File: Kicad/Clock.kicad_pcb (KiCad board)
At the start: 2 copper layers, 99 x 57.5 mm, 42 parts, among them J1 AVR-ISP-6, J2 USB_B_Micro, Q5 BC848, Q6 BC848C, Q7 BC858A, SW1 Inc, SW2 Prgm, U1 KCSC02-123, U2 KCSC02-123, U3 KCSC02-123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

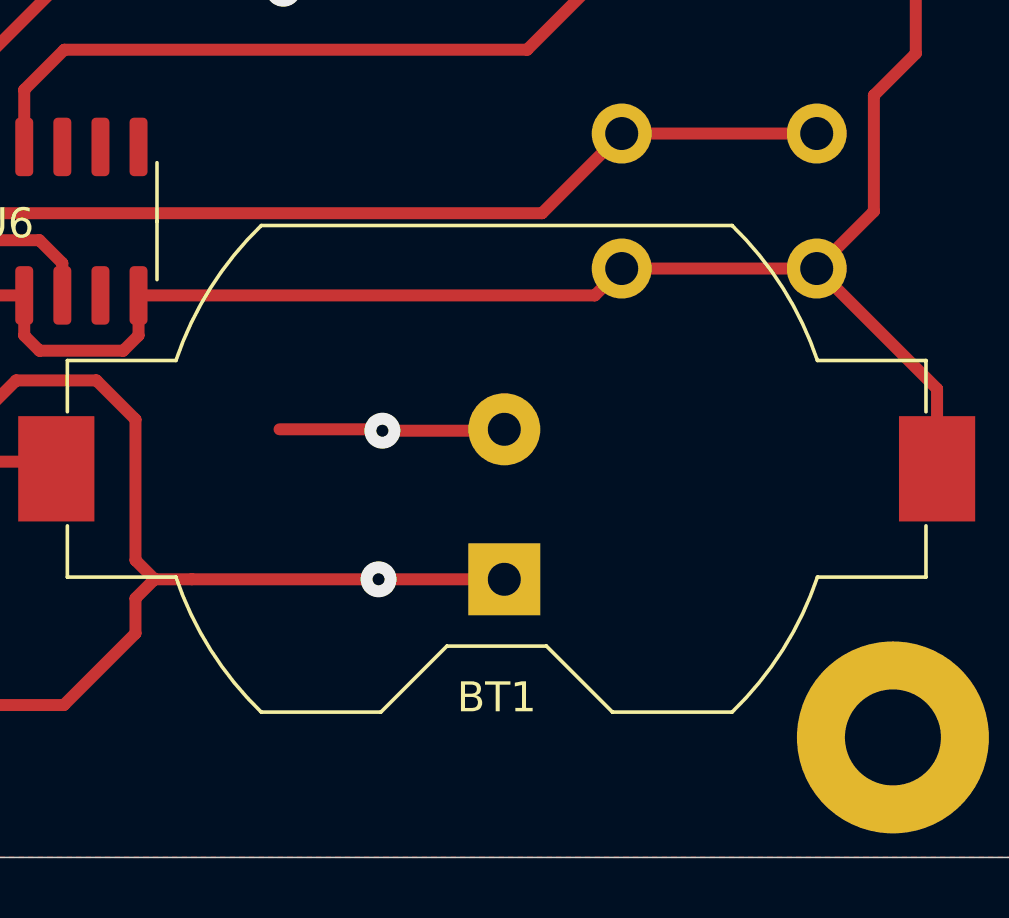
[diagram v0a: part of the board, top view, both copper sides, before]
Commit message: Flip Supercap to other board side
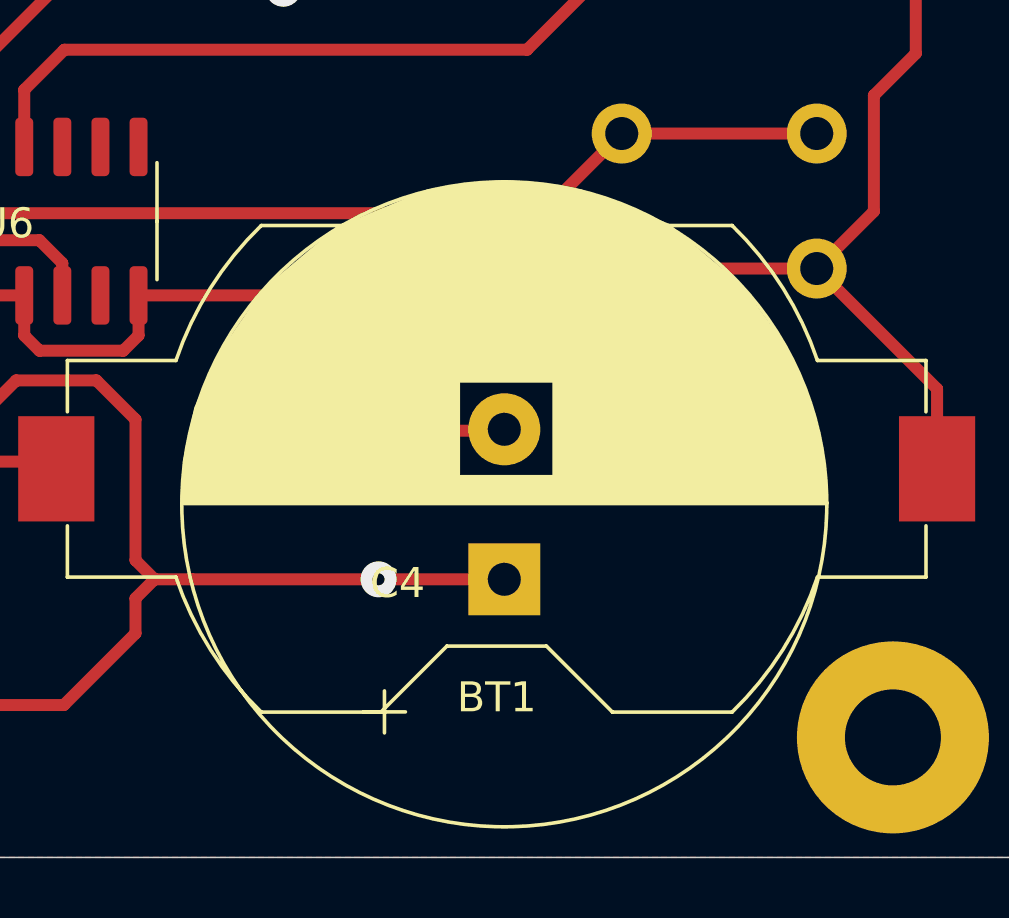
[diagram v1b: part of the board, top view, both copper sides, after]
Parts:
- C4: moved to F.Cu
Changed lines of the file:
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@@
     )
   )
-  (module Capacitor_THT:CP_Radial_D14.0mm_P5.00mm (layer B.Cu)
+  (module Capacitor_THT:CP_Radial_D14.0mm_P5.00mm (layer F.Cu)
     (at 148.3995 118.0465 90)
     (descr "CP, Radial series, Radial, pin pitch=5.00mm, , diameter=14mm, Electrolytic Capacitor")
     (tags "CP Radial series Radial pin pitch 5.00mm  diameter 14mm Electrolytic Capacitor")
-    (fp_text reference C4 (at -0.127 3.556) (layer B.SilkS)
-      (effects (font (size 1 1) (thickness 0.15)) (justify mirror))
+    (fp_text reference C4 (at -0.127 -3.556) (layer F.SilkS)
+      (effects (font (size 1 1) (thickness 0.15)))
     )
-    (fp_text value 1F (at 2.5 -8.25 270) (layer B.Fab)
-      (effects (font (size 1 1) (thickness 0.15)) (justify mirror))
+    (fp_text value 1F (at 2.5 8.25 90) (layer F.Fab)
+      (effects (font (size 1 1) (thickness 0.15)))
     )
-    (fp_line (start -4.419543 4.695) (end -4.419543 3.295) (layer B.SilkS) (width 0.12))
-    (fp_line (start -5.119543 3.995) (end -3.719543 3.995) (layer B.SilkS) (width 0.12))
-    (fp_line (start -2.813066 3.7675) (end -2.813066 2.3675) (layer B.Fab) (width 0.1))
-    (fp_line (start -3.513066 3.0675) (end -2.113066 3.0675) (layer B.Fab) (width 0.1))
-    (fp_circle (center 2.5 0) (end 13.5 0) (layer B.CrtYd) (width 0.05))
-    (fp_circle (center 2.5 0) (end 13.25 0) (layer B.SilkS) (width 0.12))
-    (fp_circle (center 2.5 0) (end 13 0) (layer B.Fab) (width 0.1))
-    (fp_line (start 2.54 10.668) (end 2.54 -10.75) (layer B.SilkS) (width 0.15))
-    (fp_poly (pts (xy 6.604 1.524) (xy 2.54 1.524) (xy 2.54 10.668) (xy 3.937 10.668)
-      (xy 5.715 10.287) (xy 7.62 9.398) (xy 9.652 8.001) (xy 11.684 5.588)
-      (xy 12.954 2.54) (xy 13.25 0) (xy 12.954 -2.54) (xy 11.811 -5.461)
-      (xy 9.779 -7.874) (xy 7.874 -9.271) (xy 5.969 -10.16) (xy 3.683 -10.668)
-      (xy 2.54 -10.668) (xy 2.54 -1.651) (xy 2.54 1.4732) (xy 3.429 1.4478)
-      (xy 3.429 -1.651) (xy 6.604 -1.651)) (layer B.SilkS) (width 0.1))
+    (fp_line (start -4.419543 -4.695) (end -4.419543 -3.295) (layer F.SilkS) (width 0.12))
+    (fp_line (start -5.119543 -3.995) (end -3.719543 -3.995) (layer F.SilkS) (width 0.12))
+    (fp_line (start -2.813066 -3.7675) (end -2.813066 -2.3675) (layer F.Fab) (width 0.1))
+    (fp_line (start -3.513066 -3.0675) (end -2.113066 -3.0675) (layer F.Fab) (width 0.1))
+    (fp_circle (center 2.5 0) (end 13.5 0) (layer F.CrtYd) (width 0.05))
+    (fp_circle (center 2.5 0) (end 13.25 0) (layer F.SilkS) (width 0.12))
+    (fp_circle (center 2.5 0) (end 13 0) (layer F.Fab) (width 0.1))
+    (fp_line (start 2.54 -10.668) (end 2.54 10.75) (layer F.SilkS) (width 0.15))
+    (fp_poly (pts (xy 6.604 -1.524) (xy 2.54 -1.524) (xy 2.54 -10.668) (xy 3.937 -10.668)
+      (xy 5.715 -10.287) (xy 7.62 -9.398) (xy 9.652 -8.001) (xy 11.684 -5.588)
+      (xy 12.954 -2.54) (xy 13.25 0) (xy 12.954 2.54) (xy 11.811 5.461)
+      (xy 9.779 7.874) (xy 7.874 9.271) (xy 5.969 10.16) (xy 3.683 10.668)
+      (xy 2.54 10.668) (xy 2.54 1.651) (xy 2.54 -1.4732) (xy 3.429 -1.4478)
+      (xy 3.429 1.651) (xy 6.604 1.651)) (layer F.SilkS) (width 0.1))
     (pad 2 thru_hole circle (at 5 0 90) (size 2.4 2.4) (drill 1.1) (layers *.Cu *.Mask)
       (net 1 GND))
